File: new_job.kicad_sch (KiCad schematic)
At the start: 87 parts, among them J1 PWM_OUT, J10 PWM_OUT, J11 Conn_01x03_Pin, J2 PWM_OUT, J3 PWM_OUT, J4 PWM_OUT, J5 PWM_OUT, J6 PWM_OUT, J7 PWM_OUT, J8 PWM_OUT, J9 Conn_01x06_Pin, K1 SANYOU_SRD_Form_C, K2 SANYOU_SRD_Form_C, Q1 NMOS, Q10 2N7002H, Q11 2N7002H, Q2 NMOS, Q3 NMOS, Q4 NMOS, Q5 NMOS, Q6 NMOS, Q7 NMOS, Q8 NMOS, Q9 NMOS, SW1 SW_Push, U1 STM32F030C6Tx, U10 TLP152, U2 TLP152, U3 TLP152, U4 TLP152, U5 TLP152, U6 TLP152, U7 TLP152, U8 TLP152, U9 TLP152

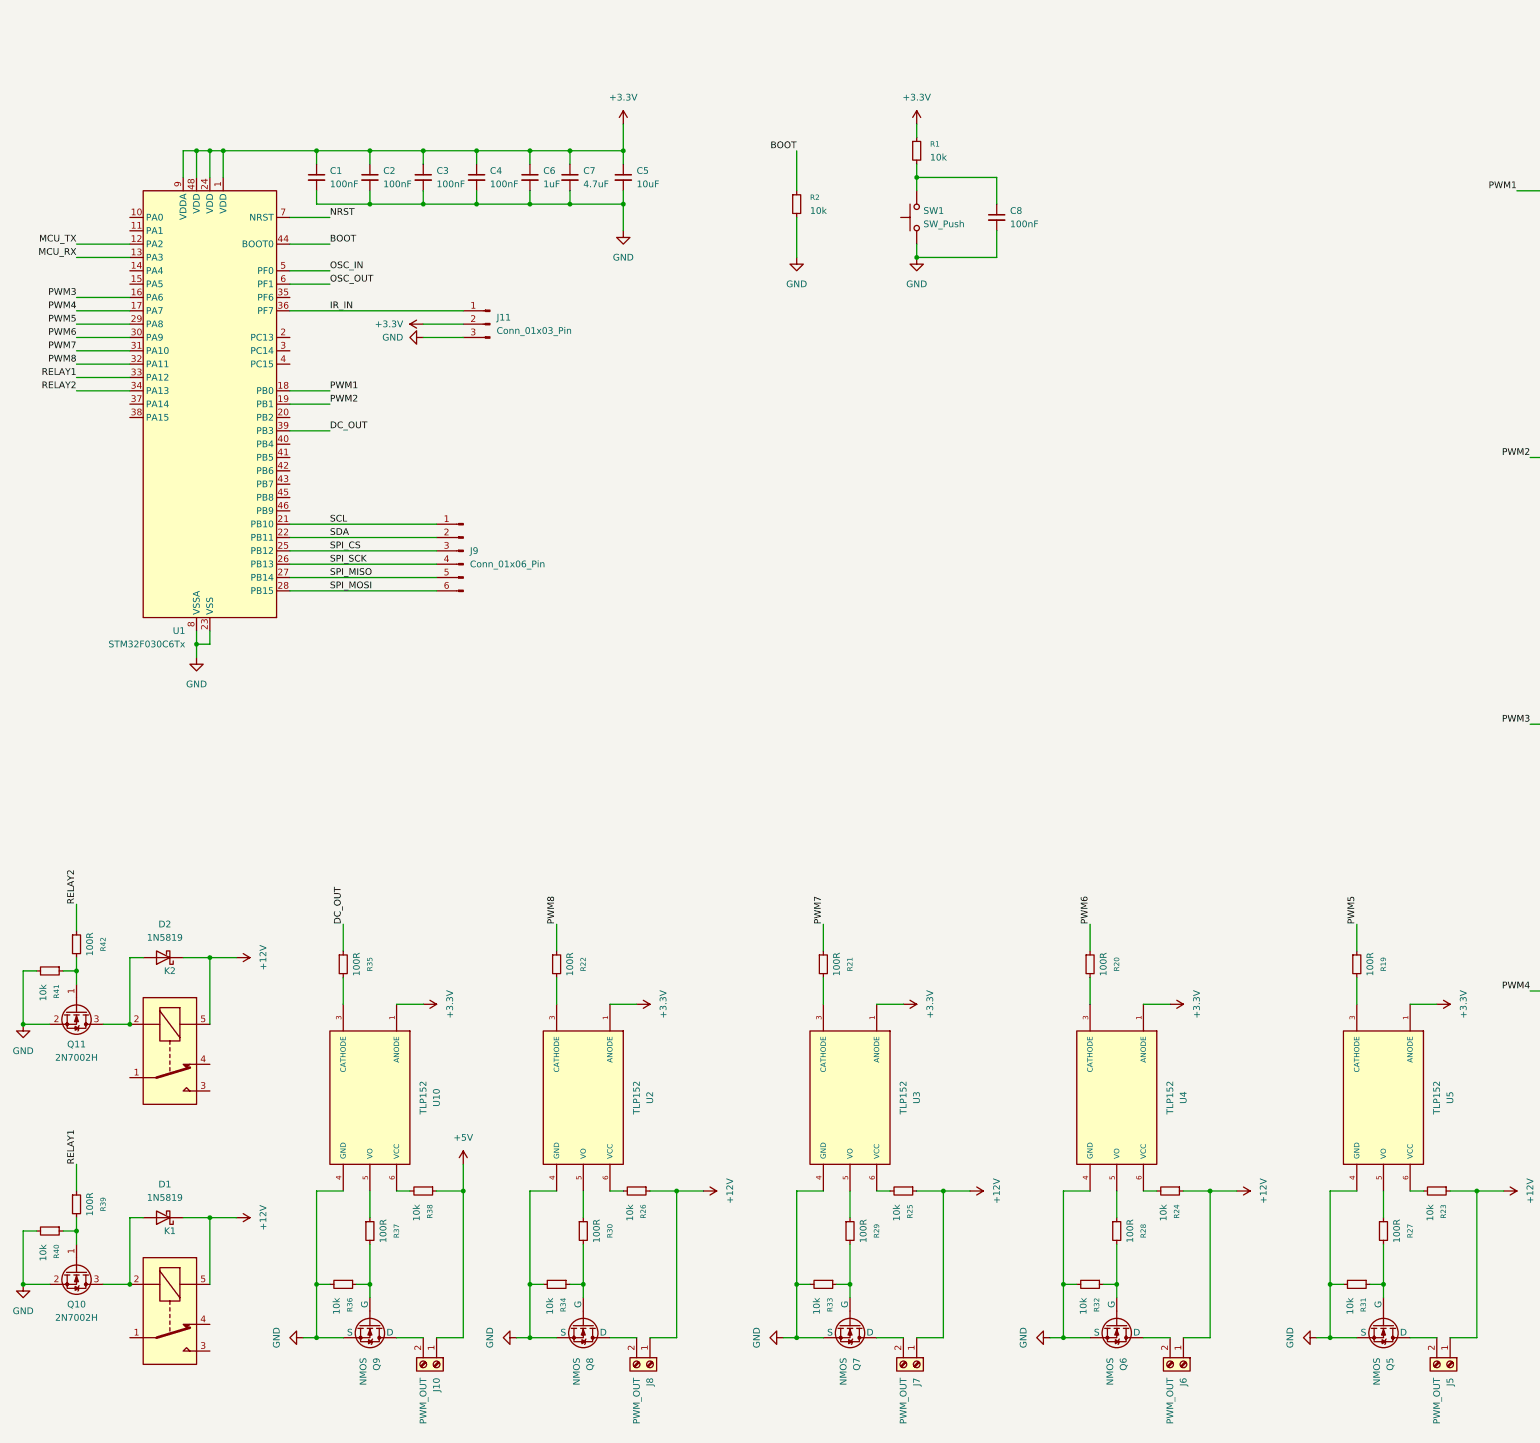
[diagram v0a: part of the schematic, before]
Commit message: crystals added
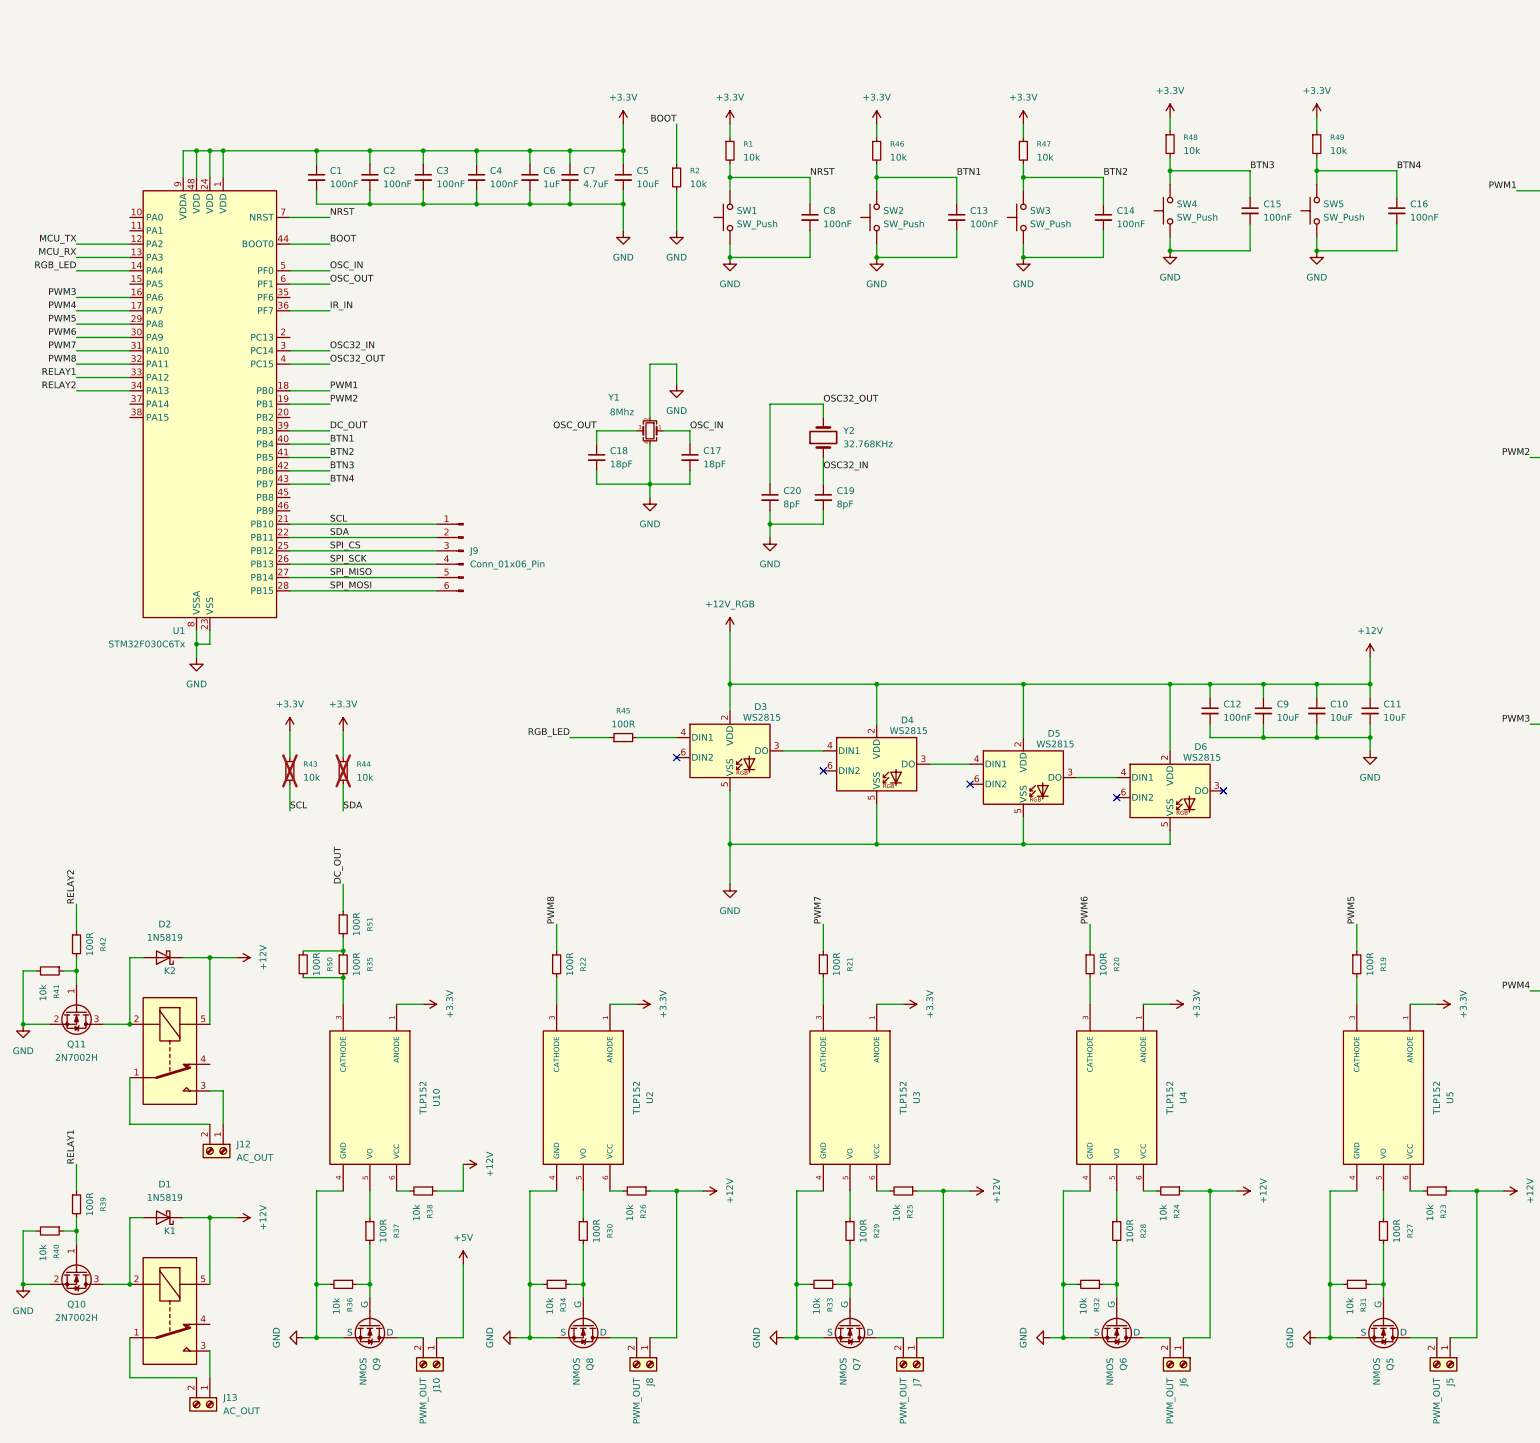
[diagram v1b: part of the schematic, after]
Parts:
- removed J11: Conn_01x03_Pin, symbol Connector:Conn_01x03_Pin
- added C10, C11, C9: 10uF, Capacitor_SMD:C_0805_2012Metric, symbol Device:C_Small
- added C12, C13, C14, C15, C16: 100nF, Capacitor_SMD:C_0402_1005Metric, symbol Device:C_Small
- added C17, C18: 18pF, symbol Device:C_Small
- added C19, C20: 8pF, symbol Device:C_Small
- added D3, D4, D5, D6: WS2815, LED_SMD:LED_WS2812_PLCC6_5.0x5.0mm_P1.6mm, symbol LED:Inolux_IN-PI556FCH
- added J12, J13: AC_OUT, Connector_Molex:Molex_SL_171971-0002_1x02_P2.54mm_Vertical, symbol Connector:Screw_Terminal_01x02
- added R43, R44, R46, R47, R48, R49: 10k, Resistor_SMD:R_0402_1005Metric, symbol Device:R_Small
- added R45, R50, R51: 100R, Resistor_SMD:R_0402_1005Metric, symbol Device:R_Small
- added SW2, SW3, SW4, SW5: SW_Push, Button_Switch_SMD:SW_SPST_B3S-1000, symbol Switch:SW_Push
- added Y1: 8Mhz, Crystal:Crystal_SMD_3225-4Pin_3.2x2.5mm, symbol Device:Crystal_GND24_Small
- added Y2: 32.768KHz, Crystal:Crystal_SMD_3215-2Pin_3.2x1.5mm, symbol Device:Crystal
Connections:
- net +12V: now also R38.1, C10.1, C11.1, C12.1, C9.1, D3.2 (VDD), D4.2 (VDD), D5.2 (VDD), D6.2 (VDD)
- net +3.3V: now also R43.1, R44.1, R46.1, R47.1, R48.1, R49.1
- net +5V: no longer R38.1
- net DC_OUT: now also R51.1; no longer R35.1
- net GND: now also C10.2, C11.2, C12.2, C13.2, C14.2, C15.2, C16.2, C17.2, C18.2, C19.2, C20.2, C9.2, D3.5 (VSS), D4.5 (VSS), D5.5 (VSS), D6.5 (VSS), SW2.1, SW3.1, SW4.1, SW5.1, Y1.2, Y1.4
- net NRST: now also C8.1, R1.2, SW1.2
- net OSC_IN: now also C17.1, Y1.1
- net OSC_OUT: now also C18.1, Y1.3
- net SCL: now also R43.2
- net SDA: now also R44.2
- net RGB_LED: now reaches U1.14 (PA4)
- net RGB_LED: now also R45.1
- net OSC32_IN: now reaches U1.3 (PC14)
- net OSC32_IN: now also C19.1, Y2.1
- net OSC32_OUT: now reaches U1.4 (PC15)
- net OSC32_OUT: now also C20.1, Y2.2
- net BTN1: now reaches U1.40 (PB4)
- net BTN1: now also C13.1, R46.2, SW2.2
- net BTN2: now reaches U1.41 (PB5)
- net BTN2: now also C14.1, R47.2, SW3.2
- net BTN3: now reaches U1.42 (PB6)
- net BTN3: now also C15.1, R48.2, SW4.2
- net BTN4: now reaches U1.43 (PB7)
- net BTN4: now also C16.1, R49.2, SW5.2
- net at R35.2, U10.3 (CATHODE): now also R50.2
- net at K2.1: now also J12.2 (Pin_2)
- net at K2.3: now also J12.1 (Pin_1)
- net at K1.1: now also J13.2 (Pin_2)
- net at K1.3: now also J13.1 (Pin_1)
- new net: D5.3 (DO), D6.4 (DIN1)
- new net: D4.3 (DO), D5.4 (DIN1)
- new net: D3.3 (DO), D4.4 (DIN1)
- new net: D3.4 (DIN1), R45.2
- new net: R35.1, R50.1, R51.2
- no-connect marks 0 -> 5
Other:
- moved on the sheet: C8, R1, R2, SW1

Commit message: pcb started
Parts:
- removed J9: Conn_01x06_Pin, symbol Connector:Conn_01x06_Pin
- added C21, C26, C27, C28, C29, C89: 470uF, Capacitor_SMD:CP_Elec_10x10.5, symbol Device:C_Polarized_Small
- added C22, C39, C40, C41, C42, C45, C53, C54, C55, C64, C65, C66, C74, C75, C76, C77, C86, C87, C88, C90, C92, C93: 100nF, Capacitor_SMD:C_0402_1005Metric, symbol Device:C_Small
- added C23, C36, C37, C38, C48, C49, C50, C61, C62, C63, C71, C72, C73, C83, C84, C85, C91, C94: 1uF, Capacitor_SMD:C_0402_1005Metric, symbol Device:C_Small
- added C24, C33, C34, C35, C51, C52, C59, C60, C69, C70, C81, C82: 4.7uF, Capacitor_SMD:C_0201_0603Metric, symbol Device:C_Small
- added C25, C30, C31, C32, C43, C44, C46, C47, C56, C57, C58, C67, C68, C78, C79, C80: 10uF, Capacitor_SMD:C_0805_2012Metric, symbol Device:C_Small
- added D7, D8, D9: 1N5819, Diode_SMD:D_SOD-123, symbol Diode:1N5819
- added F1: 630mA, Fuse:Fuse_0603_1608Metric, symbol Device:Fuse_Small
- added J11, J14: AC_OUT, Connector_Molex:Molex_SL_171971-0002_1x02_P2.54mm_Vertical, symbol Connector:Screw_Terminal_01x02
- added J15: SPK, Connector_Molex:Molex_SL_171971-0002_1x02_P2.54mm_Vertical, symbol Connector:Screw_Terminal_01x02
- added J16: LEVEL_LOW, Connector_Molex:Molex_SL_171971-0002_1x02_P2.54mm_Vertical, symbol Connector:Screw_Terminal_01x02
- added J17, J18: LEVEL_HIGH, Connector_Molex:Molex_SL_171971-0002_1x02_P2.54mm_Vertical, symbol Connector:Screw_Terminal_01x02
- added J19: VIN, Connector_Molex:Molex_SL_171971-0002_1x02_P2.54mm_Vertical, symbol Connector:Screw_Terminal_01x02
- added J20: Conn_01x04_Pin, Connector_PinHeader_2.54mm:PinHeader_1x04_P2.54mm_Vertical, symbol Connector:Conn_01x04_Pin
- added J21: IR, Connector_PinHeader_2.54mm:PinHeader_1x03_P2.54mm_Vertical, symbol Connector:Conn_01x03_Pin
- added J9: Conn_01x10_Pin, Connector_PinHeader_2.54mm:PinHeader_1x10_P2.54mm_Vertical, symbol Connector:Conn_01x10_Pin
- added K3, K4: SANYOU_SRD_Form_C, Relay_THT:Relay_SPDT_SANYOU_SRD_Series_Form_C, symbol Relay:SANYOU_SRD_Form_C
- added L1, L2: 2.2uH, Inductor_SMD:L_APV_ANR4010, symbol Device:L
- added Q12, Q13: 2N7002H, Package_TO_SOT_SMD:SOT-23, symbol Transistor_FET:2N7002H
- added R52, R53, R74, R75, R76, R77, R78, R79, R81, R82, R84: 10k, Resistor_SMD:R_0402_1005Metric, symbol Device:R_Small
- added R54, R55, R56, R57, R58, R59, R60, R61, R62, R63, R64, R65, R66, R67, R68, R69, R70, R71, R72, R73: 100R, Resistor_SMD:R_0402_1005Metric, symbol Device:R_Small
- added R80: 45.3k, Resistor_SMD:R_0402_1005Metric, symbol Device:R_Small
- added R83: 75k, Resistor_SMD:R_0402_1005Metric, symbol Device:R_Small
- added U11: DFR0299, dfrobot:MODULE_DFR0299, symbol dfrobot:DFR0299
- added U12, U13: RY9130, Package_TO_SOT_SMD:SOT-23-6, symbol RY9130:RY9130
- C17, C18: footprint (none) -> Capacitor_SMD:C_0402_1005Metric; LCSC Part (none) -> C5137554; LCSC Price (none) -> 0.0008
- C19, C20: footprint (none) -> Capacitor_SMD:C_0402_1005Metric; LCSC Part (none) -> C5448809; LCSC Price (none) -> 0.0008
- D5, D6: now not fitted
- Q1, Q2, Q3, Q4, Q5, Q6, Q7, Q8, Q9: value NMOS -> IRFR220
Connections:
- net +12V: now also C26.1, C27.1, C28.1, C29.1, C30.1, C31.1, C32.1, C33.1, C34.1, C35.1, C36.1, C37.1, C38.1, C39.1, C40.1, C41.1, C42.1, C43.1, C56.1, C57.1, C58.1, C59.1, C60.1, C61.1, C62.1, C63.1, C64.1, C65.1, C66.1, C67.1, C68.1, C69.1, C70.1, C71.1, C72.1, C73.1, C74.1, C75.1, C76.1, D7.1 (K), D8.1 (K), F1.2, K3.5, K4.5, R81.1, R82.1, U12.5 (IN), U13.5 (IN)
- net +3.3V: now also C44.1, C46.1, C47.1, C48.1, C49.1, C50.1, C51.1, C52.1, C53.1, C54.1, C55.1, C90.1, C91.1, C92.1, C93.1, C94.1, J20.1 (Pin_1), J21.1 (Pin_1), L1.2, R74.1, R75.1, R76.1, R77.1, R78.1, R80.1
- net +5V: now also C21.1, C22.1, C23.1, C24.1, C25.1, C78.1, C79.1, C80.1, C81.1, C82.1, C83.1, C84.1, C85.1, C86.1, C87.1, C88.1, C89.1, L2.2, R83.1, U11.1 (VCC)
- net GND: now also C21.2, C22.2, C23.2, C24.2, C25.2, C26.2, C27.2, C28.2, C29.2, C30.2, C31.2, C32.2, C33.2, C34.2, C35.2, C36.2, C37.2, C38.2, C39.2, C40.2, C41.2, C42.2, C43.2, C44.2, C46.2, C47.2, C48.2, C49.2, C50.2, C51.2, C52.2, C53.2, C54.2, C55.2, C56.2, C57.2, C58.2, C59.2, C60.2, C61.2, C62.2, C63.2, C64.2, C65.2, C66.2, C67.2, C68.2, C69.2, C70.2, C71.2, C72.2, C73.2, C74.2, C75.2, C76.2, C78.2, C79.2, C80.2, C81.2, C82.2, C83.2, C84.2, C85.2, C86.2, C87.2, C88.2, C89.2, C90.2, C91.2, C92.2, C93.2, C94.2, D9.2 (A), J16.2 (Pin_2), J17.2 (Pin_2), J18.2 (Pin_2), J19.2 (Pin_2), J20.4 (Pin_4), J21.3 (Pin_3), Q12.2 (S), Q13.2 (S), R52.2, R53.2, R79.2, R84.2, U11.10 (GND), U11.7 (GND), U12.2 (GND), U13.2 (GND)
- net IR_IN: now also U1.11 (PA1), J21.2 (Pin_2); no longer U1.36 (PF7)
- net MCU_RX: now also R72.2
- net MCU_TX: now also R73.1
- net RELAY2: now also U1.2 (PC13); no longer U1.34 (PA13)
- net SCL: now also J9.1 (Pin_1)
- net SDA: now also J9.2 (Pin_2)
- net SPI_CS: now also J9.3 (Pin_3)
- net SPI_MISO: now also J9.5 (Pin_5)
- net SPI_MOSI: now also J9.6 (Pin_6)
- net SPI_SCK: now also J9.4 (Pin_4)
- net at R22.2: now also R56.1, R57.1; no longer U2.3 (CATHODE)
- net at J6.2 (Pin_2): now also Q8.2 (D); no longer Q6.1 (D)
- net at R28.2, R32.1: now also Q8.1 (G); no longer Q6.2 (G)
- net at U8.3 (CATHODE): now also R62.2, R63.2; no longer R7.2
- net at U7.3 (CATHODE): now also R60.2, R61.2; no longer R11.2
- net TEMP_SENS: now reaches U1.10 (PA0)
- net TEMP_SENS: now also J18.1 (Pin_1), R76.2, R77.2, R78.2
- net GPIO2: now reaches U1.15 (PA5)
- net GPIO2: now also J9.8 (Pin_8)
- net GPIO4: now reaches U1.20 (PB2)
- net GPIO4: now also J9.10 (Pin_10)
- net RELAY3: now reaches U1.35 (PF6)
- net RELAY3: now also R54.1
- net SWCLK: now reaches U1.37 (PA14)
- net SWCLK: now also J20.3 (Pin_3)
- net GPIO3: now reaches U1.38 (PA15)
- net GPIO3: now also J9.9 (Pin_9)
- net LEVEL_LOW: now reaches U1.45 (PB8)
- net LEVEL_LOW: now also J16.1 (Pin_1), R74.2
- net LEVEL_HIGH: now reaches U1.46 (PB9)
- net LEVEL_HIGH: now also J17.1 (Pin_1), R75.2
- net at J8.2 (Pin_2): now also Q5.2 (D); no longer Q8.1 (D)
- net at U6.3 (CATHODE): now also R58.2, R59.2; no longer R12.2
- net at R6.2: now also R64.1, R65.1; no longer U9.3 (CATHODE)
- net at Q7.1 (G): now also R27.2, R31.1; no longer J7.2 (Pin_2)
- net at U4.3 (CATHODE): now also R68.1, R69.1; no longer R20.2
- net at R3.1, R4.2: now also Q1.1 (G); no longer Q1.2 (G)
- net at U3.3 (CATHODE): now also R66.1, R67.1; no longer R21.2
- net at R30.2, R34.1: now also Q5.1 (G); no longer Q8.2 (G)
- net at J2.2 (Pin_2): now also Q2.2 (D); no longer Q2.1 (D)
- net at R29.2, R33.1: now also Q9.1 (G); no longer Q7.2 (G)
- net at J1.2 (Pin_2): now also Q1.2 (D); no longer Q1.1 (D)
- net at J5.2 (Pin_2): now also Q7.2 (D); no longer Q5.1 (D)
- net at R36.1, R37.2: now also Q6.1 (G); no longer Q9.2 (G)
- net at R10.1, R9.2: now also Q2.1 (G); no longer Q2.2 (G)
- net at J4.2 (Pin_2): now also Q4.2 (D); no longer Q4.1 (D)
- net at R16.2, R18.1: now also Q4.1 (G); no longer Q4.2 (G)
- net at J10.2 (Pin_2): now also Q6.2 (D); no longer Q9.1 (D)
- net at R15.2, R17.1: now also Q3.1 (G); no longer Q3.2 (G)
- net at U5.3 (CATHODE): now also R70.1, R71.1; no longer R19.2
- net at J3.2 (Pin_2): now also Q3.2 (D); no longer Q3.1 (D)
- new net: J11.1 (Pin_1), K4.3
- new net: J11.2 (Pin_2), K4.1
- new net: R64.2, R65.2, U9.3 (CATHODE)
- new net: R19.2, R70.2, R71.2
- new net: D8.2 (A), K4.2, Q13.3 (D)
- new net: R20.2, R68.2, R69.2
- new net: C45.2, L1.1, U12.6 (SW)
- new net: R56.2, R57.2, U2.3 (CATHODE)
- new net: D9.1 (K), F1.1, J19.1 (Pin_1)
- new net: R21.2, R66.2, R67.2
- new net: C77.2, L2.1, U13.6 (SW)
- new net: J7.2 (Pin_2), Q9.2 (D)
- new net: R73.2, U11.2 (RX)
- new net: R72.1, U11.3 (TX)
- new net: C45.1, U12.1 (BS)
- new net: R79.1, R80.2, U12.3 (FB)
- new net: R81.2, U12.4 (EN)
- new net: R11.2, R60.1, R61.1
- new net: R12.2, R58.1, R59.1
- new net: R62.1, R63.1, R7.2
- new net: C77.1, U13.1 (BS)
- new net: R83.2, R84.1, U13.3 (FB)
- new net: R82.2, U13.4 (EN)
- new net: Q12.1 (G), R52.1, R54.2
- new net: D7.2 (A), K3.2, Q12.3 (D)
- new net: Q13.1 (G), R53.1, R55.2
- new net: J14.1 (Pin_1), K3.3
- new net: J14.2 (Pin_2), K3.1
- new net RELAY4: R55.1, U1.36 (PF7)
- new net SPK_DN: J15.1 (Pin_1), U11.8 (SPK2)
- new net SPK_DP: J15.2 (Pin_2), U11.6 (SPK1)
- new net SWDIO: J20.2 (Pin_2), U1.34 (PA13)
- no-connect marks 5 -> 19
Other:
- moved on the sheet: C10, C11, C12, C13, C14, C15, C16, C18, C20, C8, C9, D1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

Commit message: PCB improoved
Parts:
- removed C29: 470uF, Capacitor_SMD:CP_Elec_10x10.5, symbol Device:C_Polarized_Small
- removed C32: 10uF, Capacitor_SMD:C_0805_2012Metric, symbol Device:C_Small
- removed C34, C35, C52: 4.7uF, Capacitor_SMD:C_0201_0603Metric, symbol Device:C_Small
- removed C37, C38, C49, C50, C62, C63, C72, C73, C84, C85: 1uF, Capacitor_SMD:C_0402_1005Metric, symbol Device:C_Small
- removed C53, C64, C65, C74, C86: 100nF, Capacitor_SMD:C_0402_1005Metric, symbol Device:C_Small
- removed F1: 630mA, Fuse:Fuse_0603_1608Metric, symbol Device:Fuse_Small
- added C29: 100nF, Capacitor_SMD:C_0402_1005Metric, symbol Device:C_Small
- C24, C33, C51, C59, C60, C69, C7, C70, C81, C82: footprint Capacitor_SMD:C_0201_0603Metric -> Capacitor_SMD:C_0603_1608Metric
- J16, J17, J18: footprint Connector_Molex:Molex_SL_171971-0002_1x02_P2.54mm_Vertical -> Connector_PinHeader_2.54mm:PinHeader_1x02_P2.54mm_Vertical
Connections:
- net +12V: now also D9.1 (K), J19.1 (Pin_1), C29.1
- net GND: now also C29.2
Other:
- moved on the sheet: C48, C51, C61, C75

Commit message: production ready
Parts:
- removed C10, C11: 10uF, Capacitor_SMD:C_0805_2012Metric, symbol Device:C_Small
- removed R82: 10k, Resistor_SMD:R_0402_1005Metric, symbol Device:R_Small
- J11, J12, J13, J14: footprint Connector_Molex:Molex_SL_171971-0002_1x02_P2.54mm_Vertical -> TerminalBlock_RND:TerminalBlock_RND_205-00067_1x02_P7.50mm_Horizontal; LCSC Part (none) -> C557649; LCSC Price (none) -> 0.1631
- K1, K2, K4: LCSC Part (none) -> C30431; LCSC Price (none) -> 0.2879
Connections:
- net +12V: now also U13.4 (EN)
- net BTN1: now also U1.42 (PB6); no longer U1.40 (PB4)
- net BTN3: now also U1.40 (PB4); no longer U1.42 (PB6)
- net DC_OUT: now also J10.2 (Pin_2), Q6.2 (D); no longer R51.1, U1.39 (PB3)
- net GND: now also J9.10 (Pin_10)
- net GPIO2: now also J9.9 (Pin_9), U1.39 (PB3); no longer J9.8 (Pin_8), U1.15 (PA5)
- net GPIO3: now also J9.8 (Pin_8); no longer J9.9 (Pin_9)
- net GPIO4: now also J9.1 (Pin_1); no longer J9.10 (Pin_10)
- net PWM1: now also U1.30 (PA9); no longer U1.18 (PB0)
- net PWM2: now also U1.29 (PA8); no longer U1.19 (PB1)
- net PWM3: now also U1.31 (PA10); no longer U1.16 (PA6)
- net PWM4: now also U1.32 (PA11); no longer U1.17 (PA7)
- net PWM5: now also U1.18 (PB0); no longer U1.29 (PA8)
- net PWM6: now also U1.17 (PA7); no longer U1.30 (PA9)
- net PWM7: now also U1.16 (PA6); no longer U1.31 (PA10)
- net PWM8: now also U1.19 (PB1); no longer U1.32 (PA11)
- net RELAY1: now also U1.2 (PC13); no longer U1.33 (PA12)
- net RELAY2: now also U1.33 (PA12); no longer U1.2 (PC13)
- net SCL: now also J9.3 (Pin_3); no longer J9.1 (Pin_1)
- net SPI_CS: now also J9.4 (Pin_4); no longer J9.3 (Pin_3)
- net SPI_MISO: now also J9.6 (Pin_6); no longer J9.5 (Pin_5)
- net SPI_MOSI: now also J9.7 (Pin_7); no longer J9.6 (Pin_6)
- net SPI_SCK: now also J9.5 (Pin_5); no longer J9.4 (Pin_4)
- net SPK_DN: now also J15.2 (Pin_2); no longer J15.1 (Pin_1)
- net SPK_DP: now also J15.1 (Pin_1); no longer J15.2 (Pin_2)
- net at K4.3: now also J14.2 (Pin_2); no longer J11.1 (Pin_1)
- net at K4.1: now also J14.1 (Pin_1); no longer J11.2 (Pin_2)
- net L_OUT: now reaches C45.2, L1.1, U12.6 (SW)
- net PWM_OUT_4: now reaches J8.2 (Pin_2), Q5.2 (D)
- net PWM_OUT_3: now reaches J5.2 (Pin_2), Q7.2 (D)
- net L_OUT_5V: now reaches C77.2, L2.1, U13.6 (SW)
- net PWM_OUT_1: now reaches J7.2 (Pin_2), Q9.2 (D)
- net PWM_OUT_2: now reaches J6.2 (Pin_2), Q8.2 (D)
- net PWM_OUT_6: now reaches J3.2 (Pin_2), Q3.2 (D)
- net PWM_OUT_7: now reaches J2.2 (Pin_2), Q2.2 (D)
- net PWM_OUT_8: now reaches J1.2 (Pin_2), Q1.2 (D)
- net at J13.1 (Pin_1): now also K3.1; no longer K1.3
- net at J13.2 (Pin_2): now also K3.3; no longer K1.1
- net at J12.1 (Pin_1): now also K2.1; no longer K2.3
- net at J12.2 (Pin_2): now also K2.3; no longer K2.1
- net PWM_OUT_5: now reaches J4.2 (Pin_2), Q4.2 (D)
- new net: J11.1 (Pin_1), K1.1
- new net: J11.2 (Pin_2), K1.3
- new net DC_OUT_CMD: R51.1, U1.15 (PA5)
- no-connect marks 19 -> 18
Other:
- moved on the sheet: J12, J15, J9
